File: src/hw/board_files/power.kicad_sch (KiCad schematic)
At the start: 24 parts, among them P1 USB_C_Plug_USB2.0, SW1 SW_SPDT, U1 MCP73831-2-OT, U2 TPS63031DSKR

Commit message: Started filling out BOM
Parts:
- D2: renamed from D4; footprint LED_SMD:LED_0805_2012Metric -> LED_SMD:LED_0603_1608Metric
- U2: renamed from U1; value MCP73831-2-OT -> MCP73831T-2ACI/OT
- renumbered C7 to C1, C3 to C2, C8 to C3, C1 to C6, C6 to C7, C2 to C8, D2 to D1, D1 to D3, D3 to D4, R3 to R1, R4 to R2, R2 to R3, R1 to R4, U2 to U1

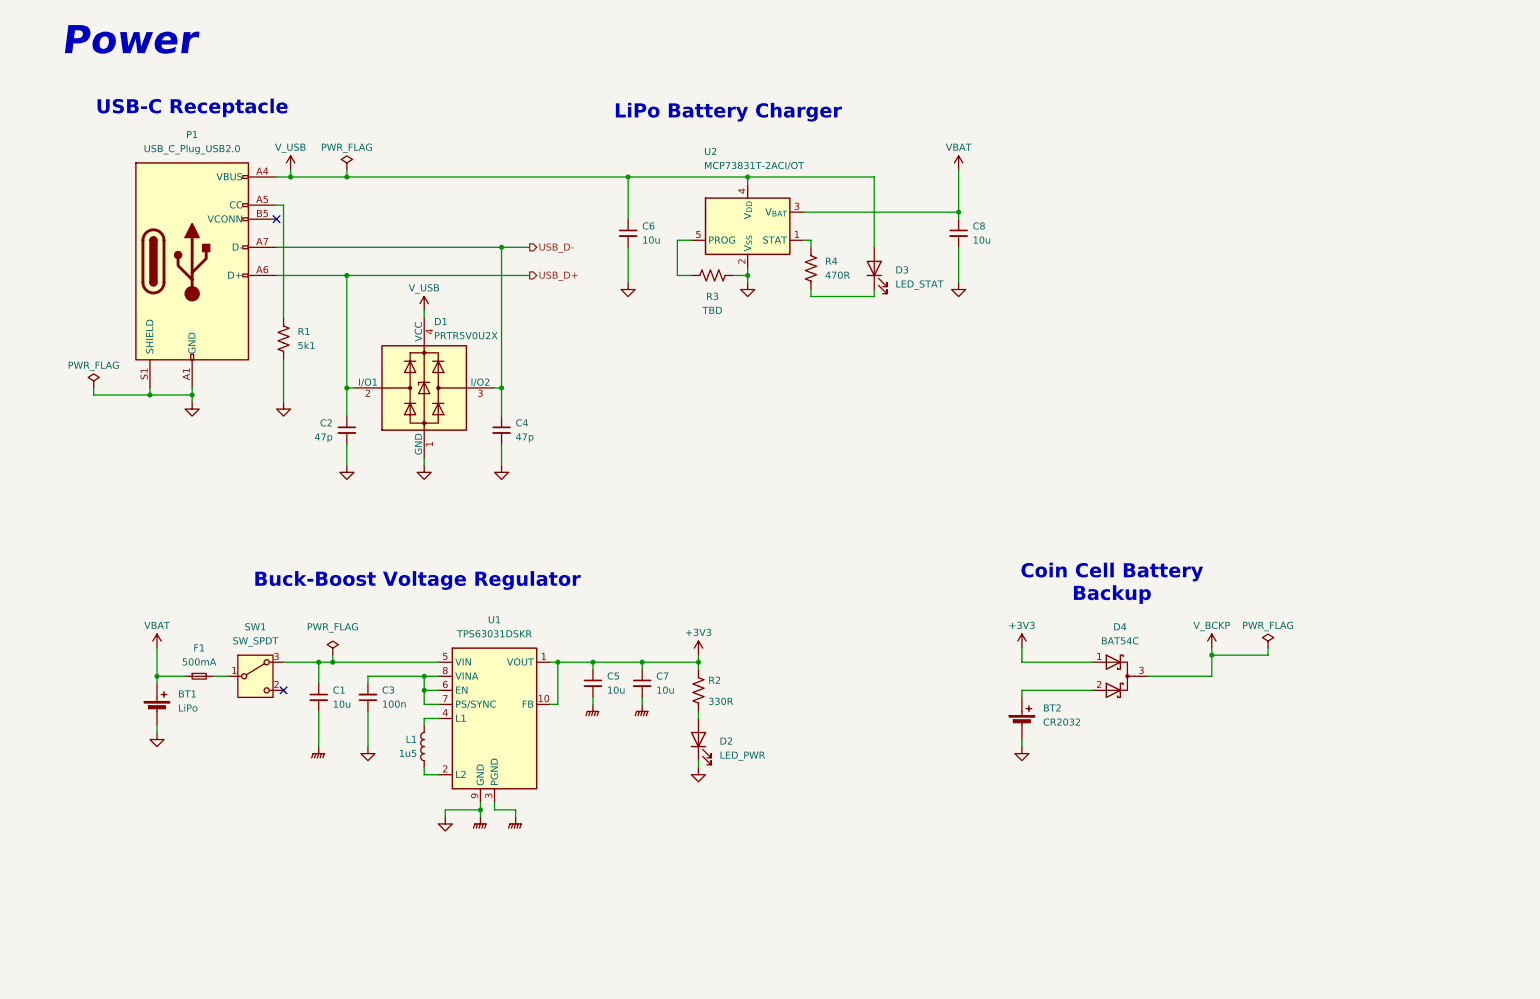
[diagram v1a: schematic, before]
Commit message: Started ESP32 schematic
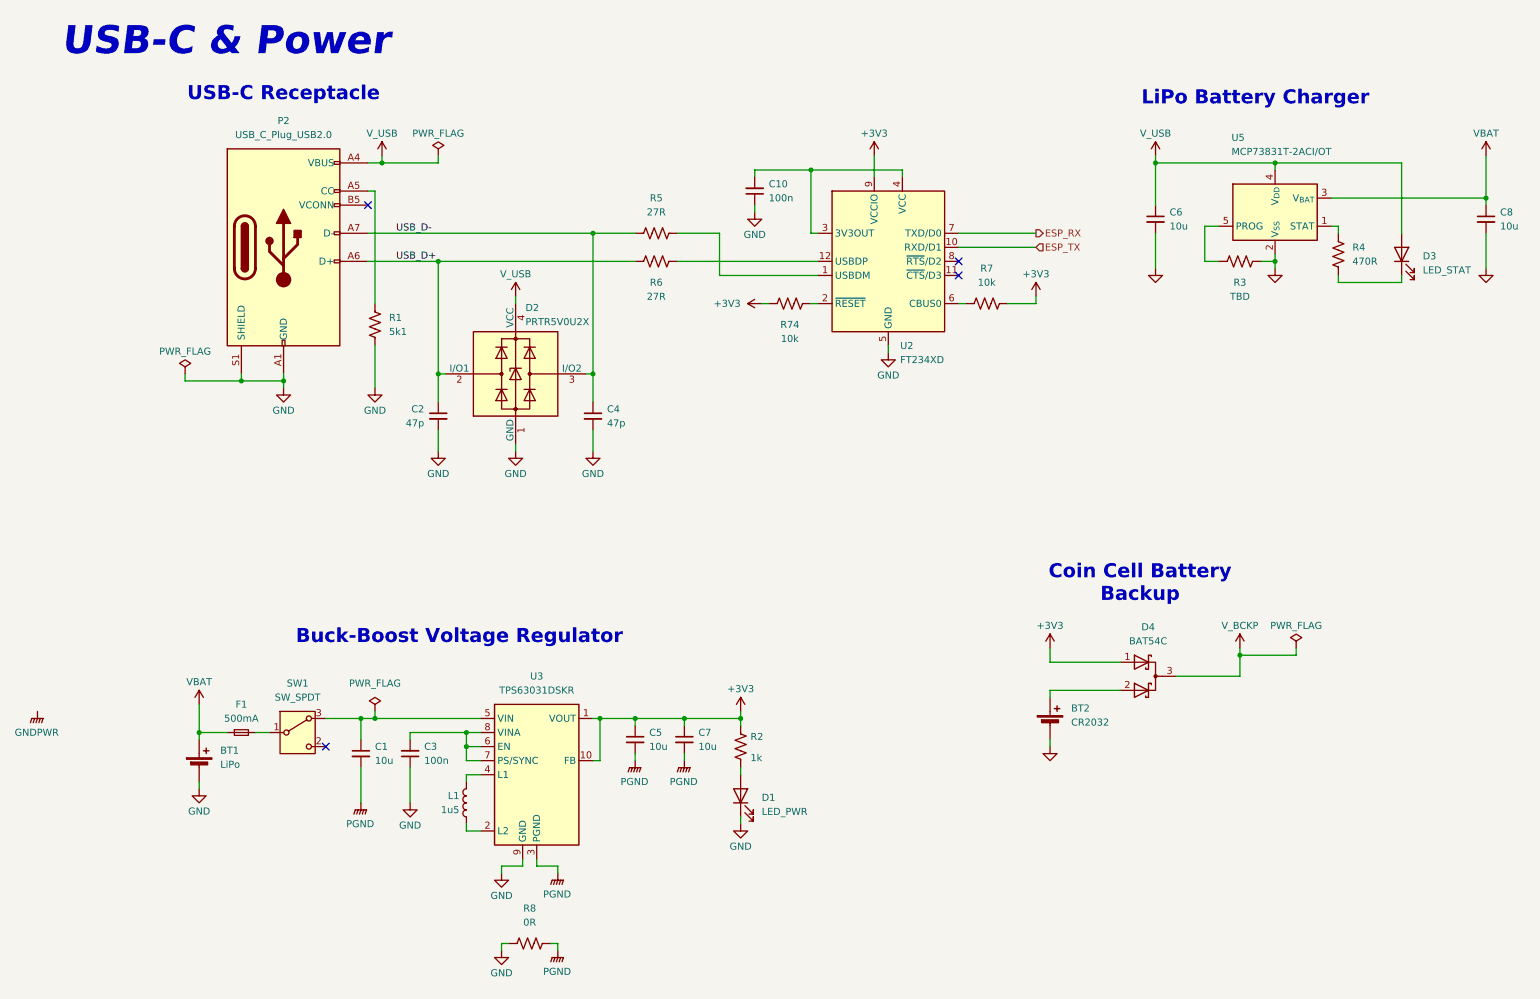
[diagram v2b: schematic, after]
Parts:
- removed D1: PRTR5V0U2X, Package_TO_SOT_SMD:SOT-143, symbol Power_Protection:PRTR5V0U2X
- removed D2: LED_PWR, LED_SMD:LED_0603_1608Metric, symbol Device:LED
- removed P1: USB_C_Plug_USB2.0, Connector_USB:USB_C_Receptacle_GCT_USB4110, symbol Connector:USB_C_Plug_USB2.0
- removed U1: TPS63031DSKR, Package_SON:WSON-10-1EP_2.5x2.5mm_P0.5mm_EP1.2x2mm, symbol Regulator_Switching:TPS63031DSK
- removed U2: MCP73831T-2ACI/OT, Package_TO_SOT_SMD:SOT-23-5, symbol Battery_Management:MCP73831-2-OT
- added C10: 100n, Capacitor_SMD:C_0603_1608Metric, symbol Device:C_Small
- added D1: LED_PWR, LED_SMD:LED_0603_1608Metric, symbol Device:LED
- added D2: PRTR5V0U2X, Package_TO_SOT_SMD:SOT-143, symbol Power_Protection:PRTR5V0U2X
- added P2: USB_C_Plug_USB2.0, Connector_USB:USB_C_Receptacle_GCT_USB4110, symbol Connector:USB_C_Plug_USB2.0
- added R5, R6: 27R, Resistor_SMD:R_0603_1608Metric, symbol Device:R_US
- added R7, R74: 10k, Resistor_SMD:R_0603_1608Metric, symbol Device:R_US
- added R8: 0R, symbol Device:R_US
- added U2: FT234XD, Package_DFN_QFN:WDFN-12-1EP_3x3mm_P0.45mm_EP1.7x2.5mm, symbol Interface_USB:FT234XD
- added U3: TPS63031DSKR, Package_SON:WSON-10-1EP_2.5x2.5mm_P0.5mm_EP1.2x2mm, symbol Regulator_Switching:TPS63031DSK
- added U5: MCP73831T-2ACI/OT, Package_TO_SOT_SMD:SOT-23-5, symbol Battery_Management:MCP73831-2-OT
- R2: value 330R -> 1k
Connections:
- net +3V3: now also R7.2, R74.2, U2.9 (VCCIO), U3.1 (VOUT), U3.10 (FB)
- net GND: now also C10.1, D1.1 (K), D2.1 (GND), P2.A1 (GND), P2.A12 (GND), P2.B1 (GND), P2.B12 (GND), P2.S1 (SHIELD), R8.1, U2.13 (GND), U2.5 (GND), U3.9 (GND), U5.2 (V_{SS}); no longer C1.2, C5.2, C7.2
- net USB_D+: now also D2.2 (I/O1), P2.A6 (D+), R6.2
- net USB_D-: now also D2.3 (I/O2), P2.A7 (D-), R5.2
- net VBAT: now also U5.3 (V_{BAT})
- net V_USB: now also D2.4 (VCC), P2.A4 (VBUS), P2.A9 (VBUS), P2.B4 (VBUS), P2.B9 (VBUS), U5.4 (V_{DD})
- net at R3.2: now also U5.5 (PROG)
- net at R1.2: now also P2.A5 (CC)
- net at R4.2: now also U5.1 (STAT)
- net at L1.1: now also U3.2 (L2)
- net at L1.2: now also U3.4 (L1)
- net at C1.1, SW1.3 (A): now also U3.5 (VIN)
- net at C3.2: now also U3.6 (EN), U3.7 (PS/SYNC), U3.8 (VINA)
- net at R2.2: now also D1.2 (A)
- new net: R6.1, U2.12 (USBDP)
- new net: R5.1, U2.1 (USBDM)
- new net: R74.1, U2.2 (~{RESET})
- new net: C10.2, U2.3 (3V3OUT), U2.4 (VCC)
- new net: R7.1, U2.6 (CBUS0)
- new net ESP_RX: U2.7 (TXD/D0)
- new net ESP_TX: U2.10 (RXD/D1)
- new net PGND: C1.2, C5.2, C7.2, R8.2, U3.11 (PGND), U3.3 (PGND)
- no-connect marks 2 -> 4
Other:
- note added: "USB-C & Power"
- note removed: "Power"
- company: B. Kuhn -> EE 333 - Electronic Systems Design
- title: Golf GPS -> Pocket Caddy
- moved on the sheet: BT1, BT2, C1, C2, C3, C4, C5, C6, C7, C8, D3, D4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

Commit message: Minor schematic changes
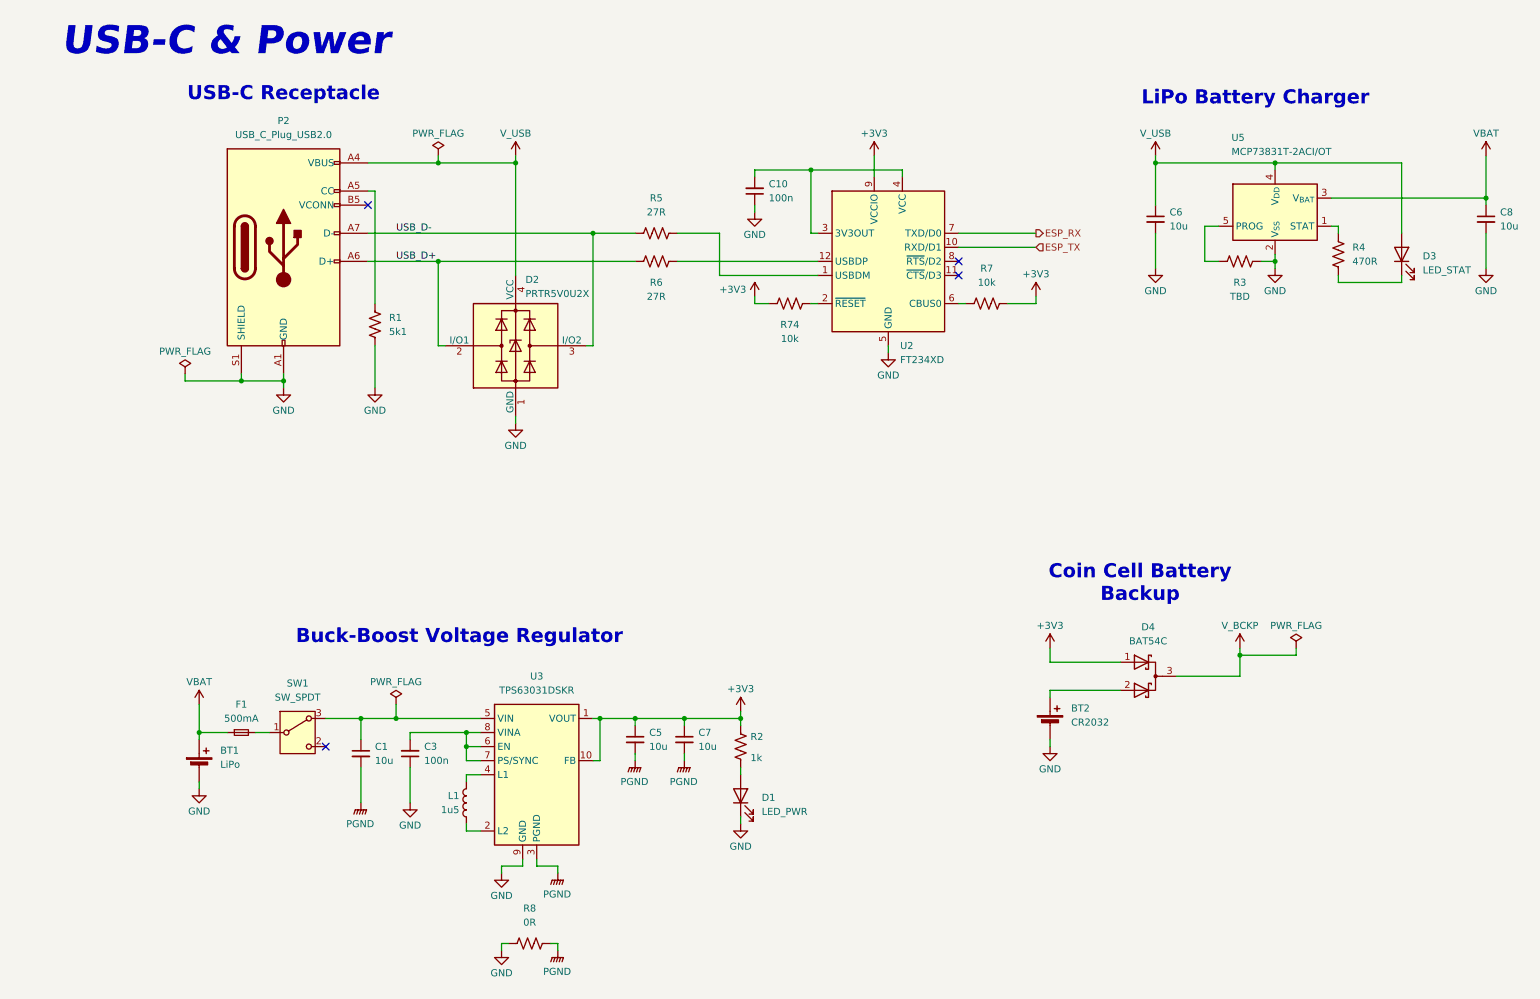
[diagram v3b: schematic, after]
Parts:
- removed C2, C4: 47p, Capacitor_SMD:C_0603_1608Metric, symbol Device:C_Small
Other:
- moved on the sheet: D2

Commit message: Sch updates
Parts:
- removed C10: 100n, Capacitor_SMD:C_0603_1608Metric, symbol Device:C_Small
- removed R5, R6: 27R, Resistor_SMD:R_0603_1608Metric, symbol Device:R_US
- removed R7, R74: 10k, Resistor_SMD:R_0603_1608Metric, symbol Device:R_US
- removed U2: FT234XD, Package_DFN_QFN:WDFN-12-1EP_3x3mm_P0.45mm_EP1.7x2.5mm, symbol Interface_USB:FT234XD
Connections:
- no-connect marks 4 -> 2
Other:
- moved on the sheet: C6, C8, D3, R3, R4, U5

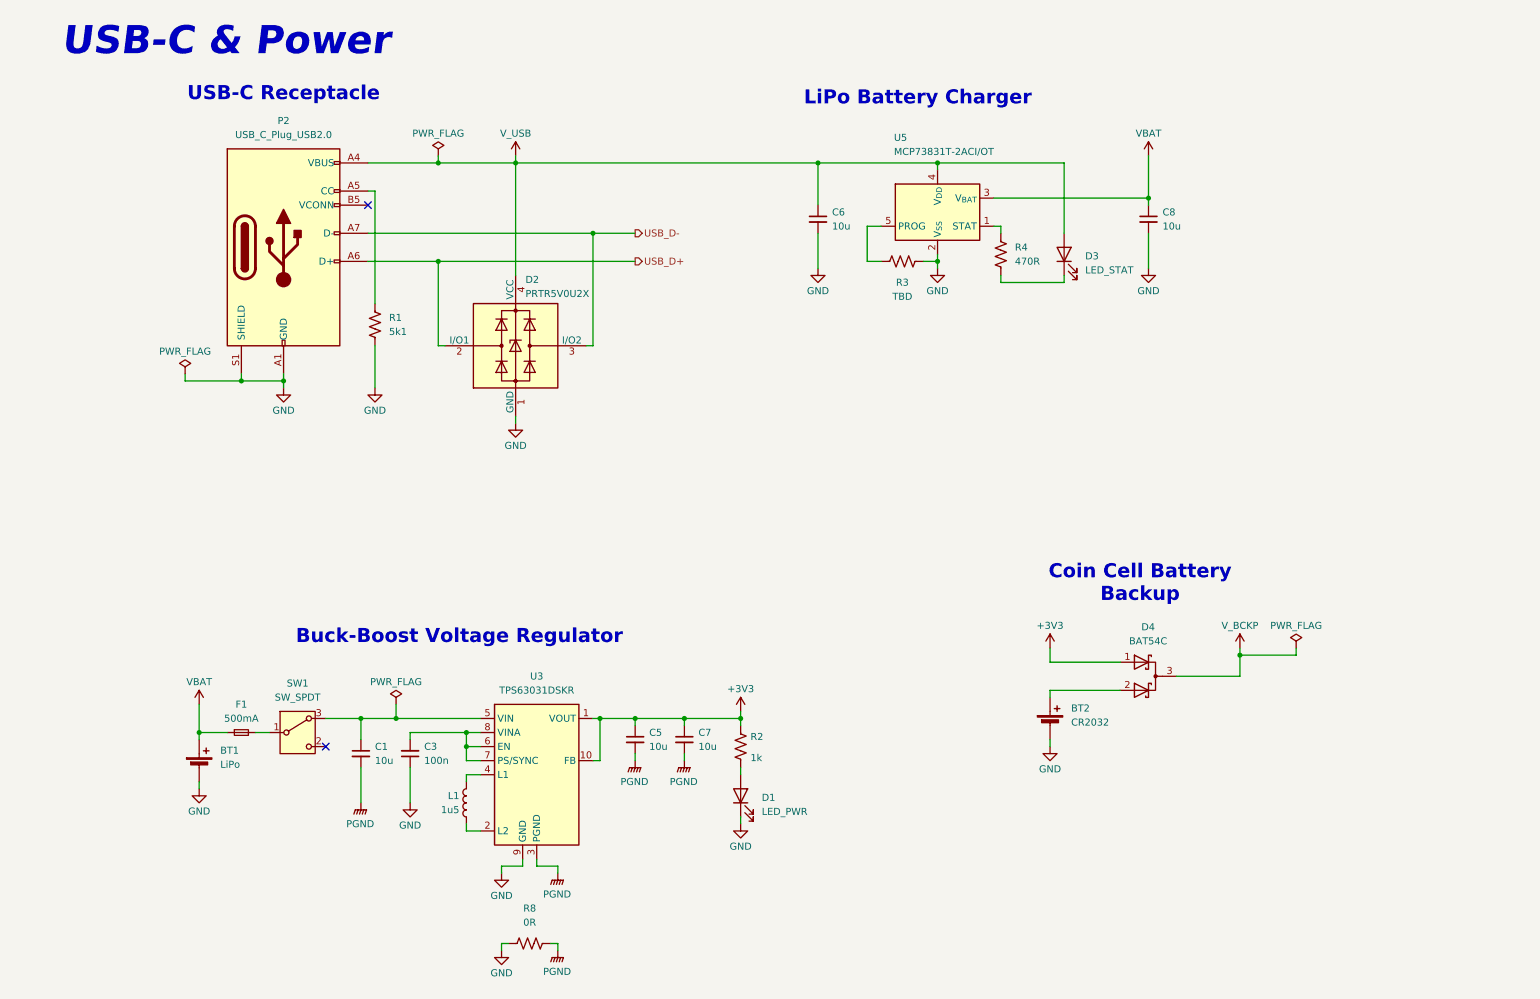
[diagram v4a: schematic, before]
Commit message: Schematic updates
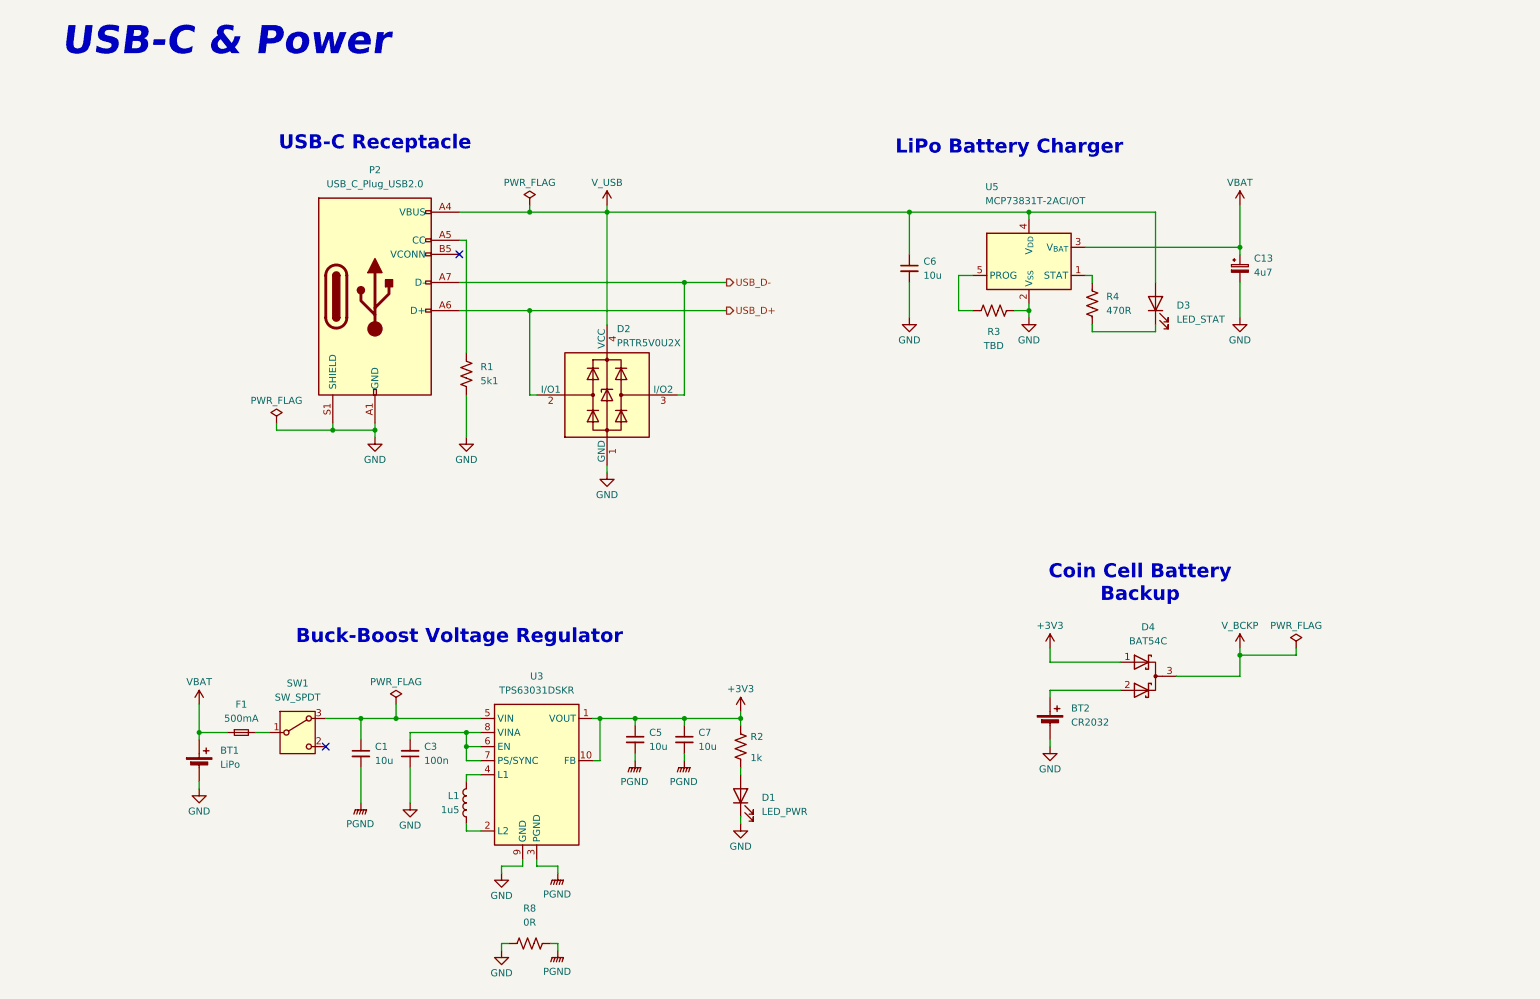
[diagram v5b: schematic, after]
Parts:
- removed C8: 10u, Capacitor_SMD:C_0603_1608Metric, symbol Device:C_Small
- added C13: 4u7, symbol Device:C_Polarized_Small
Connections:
- net GND: now also C13.2
- net VBAT: now also C13.1
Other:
- moved on the sheet: C6, D2, D3, P2, R1, R3, R4, U5
